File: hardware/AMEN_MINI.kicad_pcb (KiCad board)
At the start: 2 copper layers, 114.5 x 168.9 mm, 58 parts, among them J2 Conn_01x04_Pin, J3 Conn_01x14, J4 Conn_01x14, SW1 SW_Push_45deg, SW10 SW_Push_45deg, SW11 SW_Push_45deg, SW12 SW_Push_45deg, SW13 SW_Push_45deg, SW14 SW_Push_45deg, SW15 SW_Push_45deg, SW16 SW_Push_45deg, SW17 SW_Push_45deg, SW18 SW_Push_45deg, SW19 SW_Push_45deg, SW2 SW_Push_45deg, SW20 SW_Push_45deg, SW21 SW_Push_45deg, SW3 SW_Push_45deg, SW4 SW_Push_45deg, SW5 SW_Push_45deg, SW6 SW_Push_45deg, SW7 SW_Push_45deg, SW8 SW_Push_45deg, SW9 SW_Push_45deg, U2 Teensy4.1

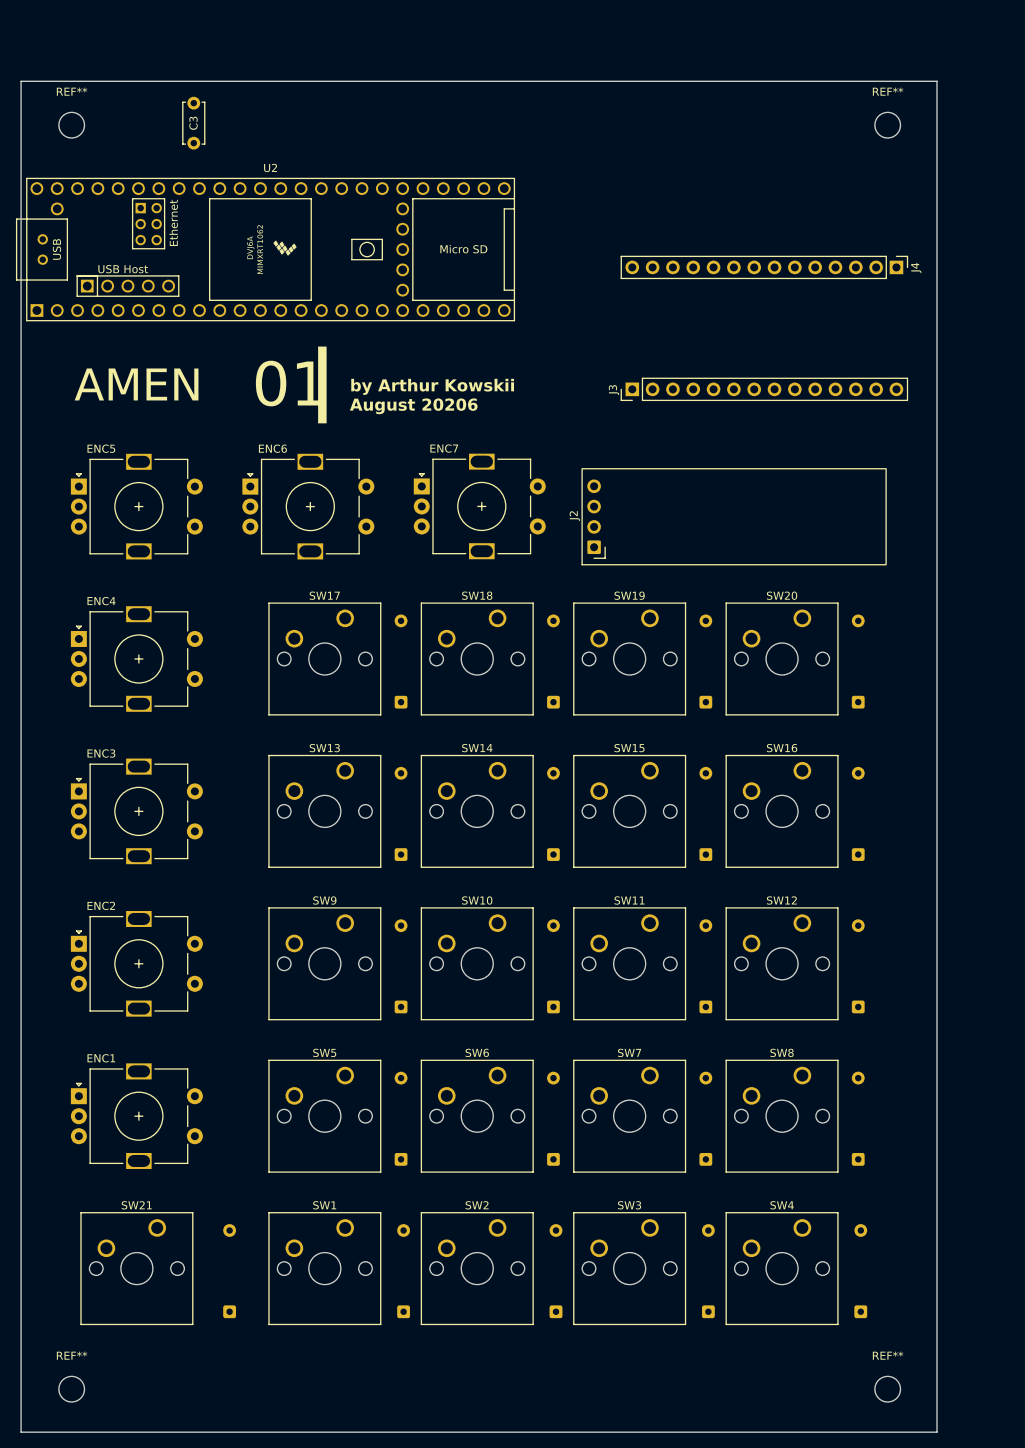
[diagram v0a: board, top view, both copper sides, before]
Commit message: Pre DRC connections
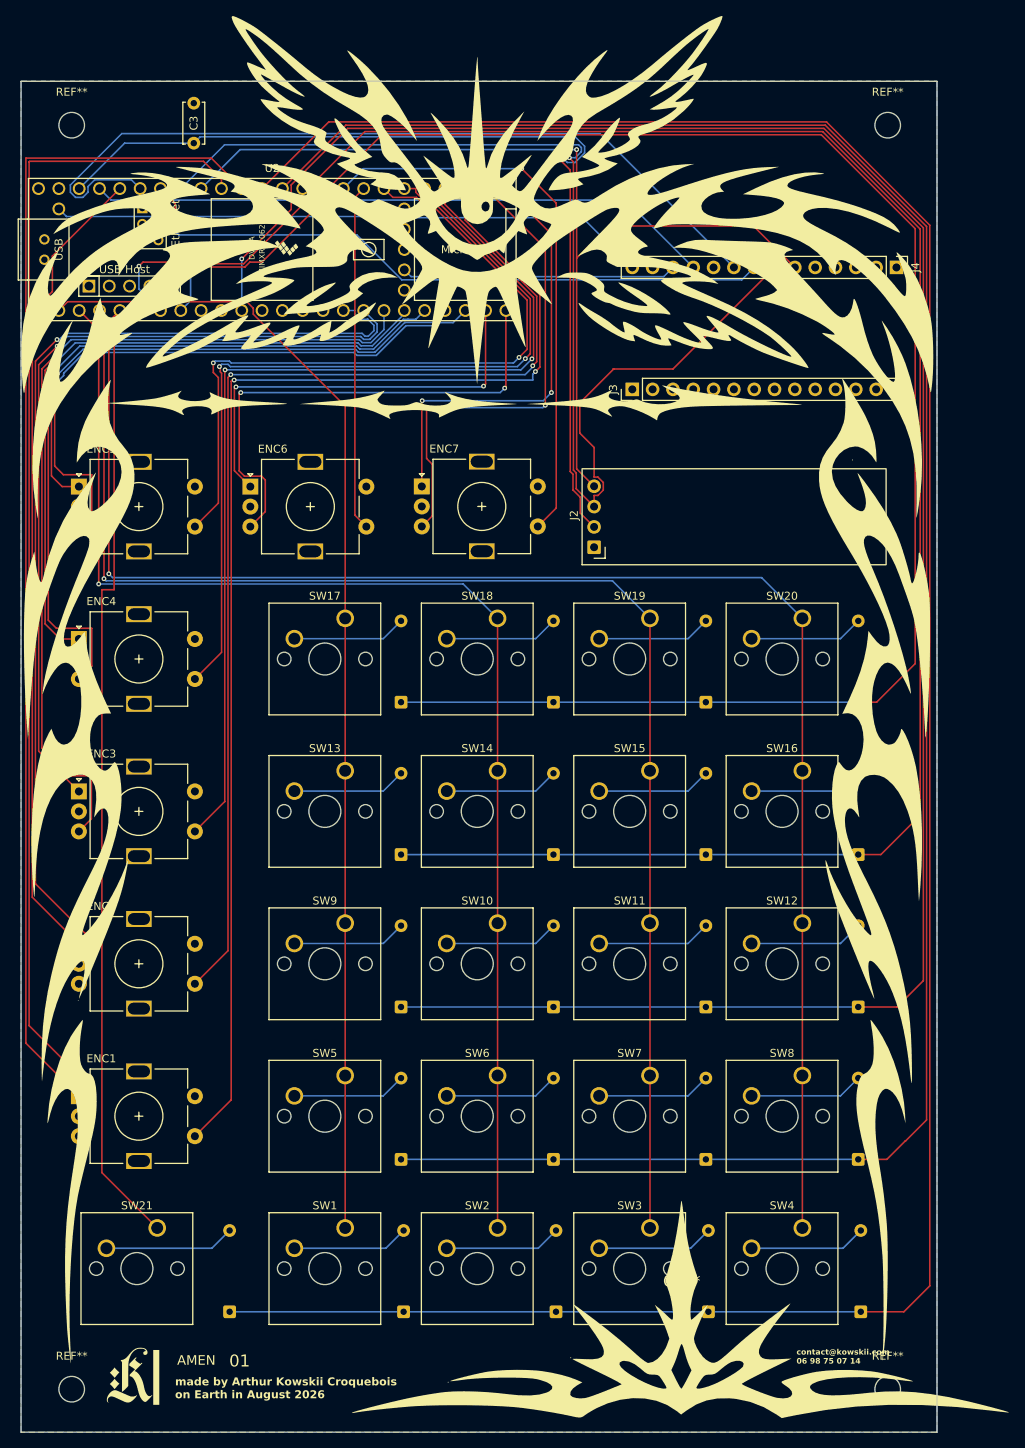
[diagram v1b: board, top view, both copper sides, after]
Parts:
- added G***: LOGO, LOGO, F.Cu at (56.2, 175.3)
- added G***: LOGO, LOGO, F.Cu at (99.7, 89.6)
- added G***: LOGO, LOGO, F.Cu at (96.6, 53.0)
- added G***: LOGO, LOGO, F.Cu at (125.3, 163.5)
- moved U2 0.20 mm to (74.1, 34.5)
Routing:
- net /ROW4: track 0.00 -> 313.7 mm
- net /ROW3: track 0.00 -> 268.5 mm
- net /ROW2: track 0.00 -> 266.1 mm, vias 0 -> 1
- net /ROW1: track 0.00 -> 250.3 mm, vias 0 -> 1
- net /ROW0: track 0.00 -> 237.4 mm, vias 0 -> 1
- net /COL3: track 0.00 -> 198.7 mm, vias 0 -> 1
- net /COL2: track 0.00 -> 180.3 mm, vias 0 -> 1
- net /COL1: track 0.00 -> 163.0 mm, vias 0 -> 1
- net /E1_SW: track 0.00 -> 162.2 mm, vias 0 -> 2
- net +3V3: track 0.00 -> 155.0 mm, vias 0 -> 2
- net /E1_B: track 0.00 -> 151.6 mm
- net /E1_A: track 0.00 -> 148.6 mm
- net /SCL: track 0.00 -> 146.4 mm, vias 0 -> 1
- net /COL0: track 0.00 -> 144.8 mm
- net /E2_SW: track 0.00 -> 143.4 mm, vias 0 -> 2
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- added copper zone on B.Cu, net GND
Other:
- board text added: "contact@kowskii.com 06 98 75 07 14"
- board text added: "made by Arthur Kowskii Croquebois on Earth in August 2026"
- board text removed: "by Arthur Kowskii August 20206"

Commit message: post DRC linking, 0 errors
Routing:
- net GND: track 0.00 -> 97.0 mm, vias 0 -> 4
- net /I2S_DOUT: track 0.00 -> 93.0 mm, vias 0 -> 1
- net /I2S_DIN: track 0.00 -> 90.1 mm, vias 0 -> 1
- net +3V3: track 155.0 -> 209.2 mm, vias 2 -> 3
- net /+5V_USB: track 74.7 -> 81.9 mm

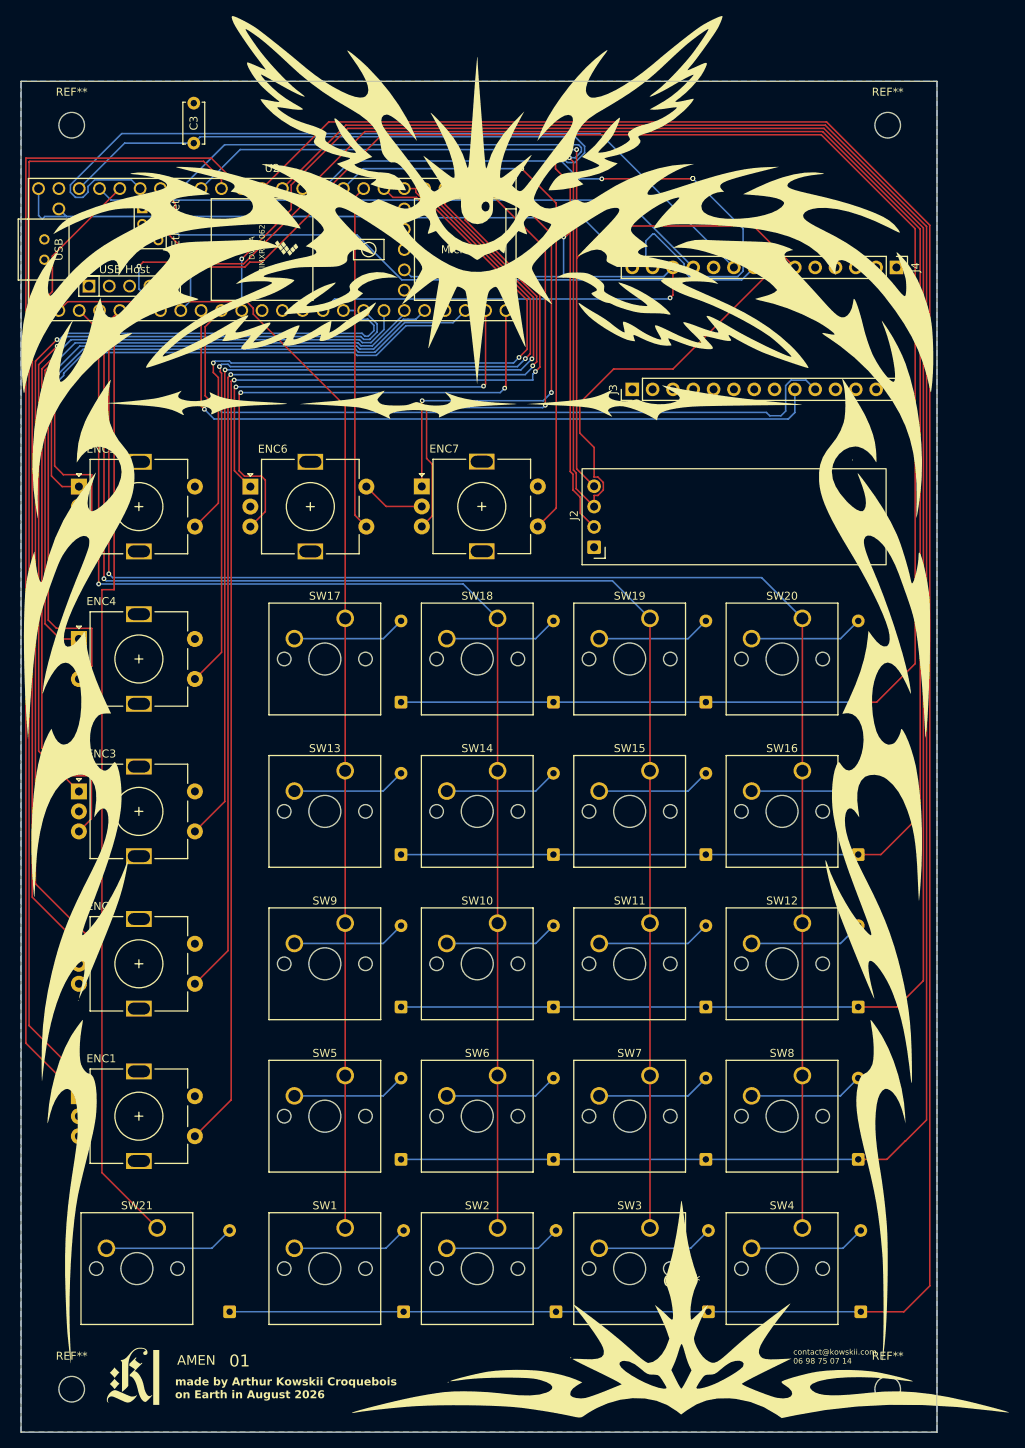
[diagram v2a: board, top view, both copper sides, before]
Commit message: fix(pcb): improve I2S routing and ground continuity
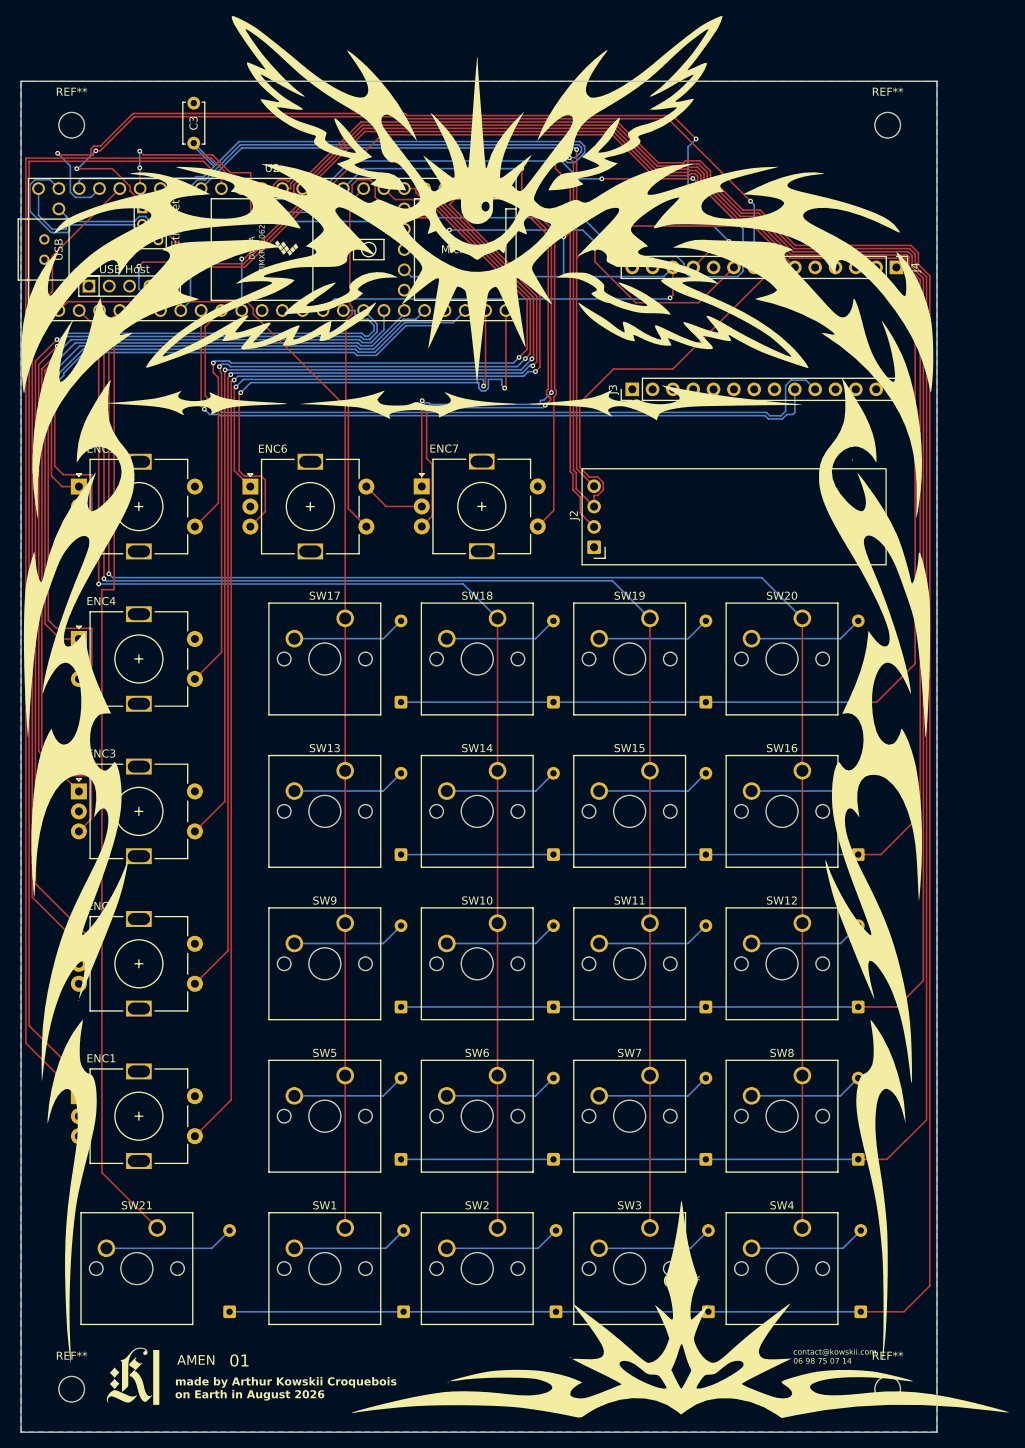
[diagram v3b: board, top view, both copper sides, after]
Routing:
- net /I2S_MCLK: track 78.3 -> 115.2 mm, vias 0 -> 3
- net /I2S_LRCLK: track 81.6 -> 112.5 mm, vias 1 -> 3
- net GND: track 97.0 -> 119.1 mm, vias 4 -> 3
- net +3V3: track 209.2 -> 216.9 mm
- net /I2S_BCLK: track 104.2 -> 97.7 mm, vias 0 -> 6
- net /+5V_USB: track 81.9 -> 85.5 mm
- net /E6_B: track 63.2 -> 66.4 mm
- net /E7_B: track 60.8 -> 63.1 mm
- net /ROW1: track 250.3 -> 248.1 mm
- net /ROW0: track 237.4 -> 235.4 mm
- net /ROW4: track 313.7 -> 312.0 mm
- net /ROW3: track 268.5 -> 266.8 mm
- net /ROW2: track 266.1 -> 264.7 mm
- net /E1_SW: track 162.2 -> 163.4 mm
- net /E6_SW: track 43.3 -> 44.5 mm
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
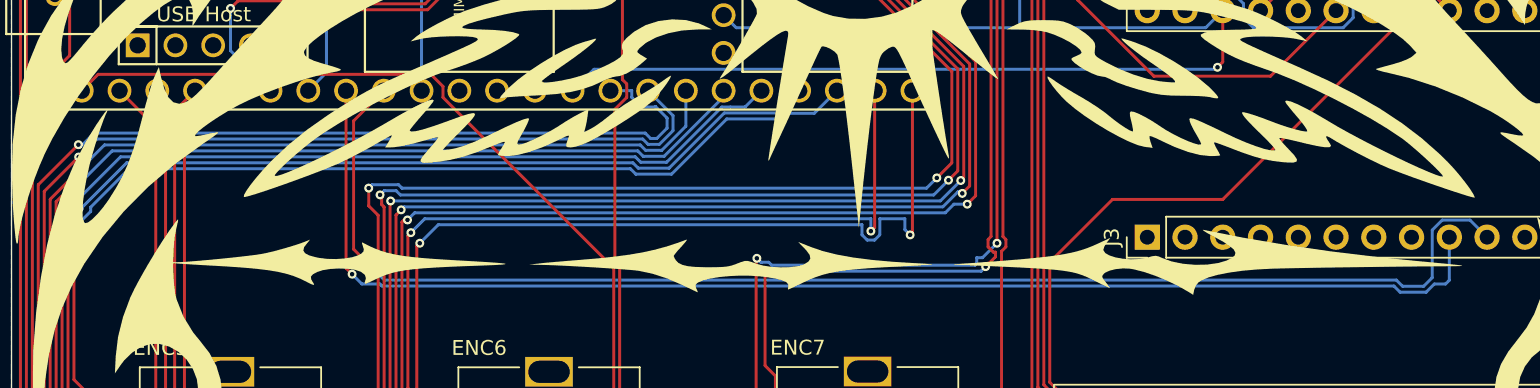
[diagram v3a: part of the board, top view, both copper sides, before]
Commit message: increasing gap between DIN & DOUT tracks
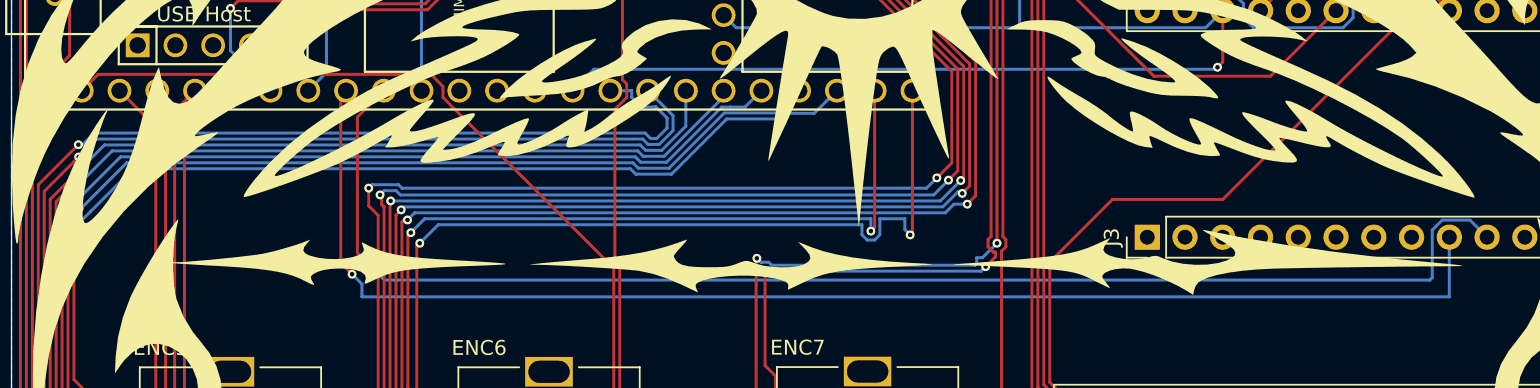
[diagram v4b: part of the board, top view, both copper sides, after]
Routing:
- net /I2S_DIN: track 90.1 -> 91.8 mm
- net /I2S_DOUT: track 93.0 -> 92.4 mm
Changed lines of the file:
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@@
-	)
-	(segment
-		(start 47.9964 50.286529)
-		(end 47.9964 50.003686)
-		(width 0.2)
-		(layer "B.Cu")
-		(net "/E5_B")
 	)
 	(segment
@@
 	)
 	(segment
+		(start 50.86773 47.4152)
+		(end 84.304259 47.4152)
+		(width 0.2)
+		(layer "B.Cu")
+		(net "/E5_B")
+	)
+	(segment
+		(start 47.9964 50.286529)
+		(end 50.86773 47.4152)
+		(width 0.2)
+		(layer "B.Cu")
+		(net "/E5_B")
+	)
+	(segment
+		(start 94.322086 44.064)
+		(end 94.698086 43.688)
+		(width 0.2)
+		(layer "B.Cu")
+		(net "/E5_B")
+	)
+	(segment
+		(start 90.786744 44.064)
+		(end 94.322086 44.064)
+		(width 0.2)
+		(layer "B.Cu")
+		(net "/E5_B")
+	)
+	(segment
+		(start 96.6724 43.688)
+		(end 98.1964 42.164)
+		(width 0.2)
+		(layer "B.Cu")
+		(net "/E5_B")
+	)
+	(segment
+		(start 84.667974 47.778914)
+		(end 87.07183 47.778914)
+		(width 0.2)
+		(layer "B.Cu")
+		(net "/E5_B")
+	)
+	(segment
 		(start 94.698086 43.688)
 		(end 96.6724 43.688)
@@
 	)
 	(segment
-		(start 96.6724 43.688)
-		(end 98.1964 42.164)
-		(width 0.2)
-		(layer "B.Cu")
-		(net "/E5_B")
-	)
-	(segment
-		(start 50.584886 47.4152)
-		(end 84.304259 47.4152)
-		(width 0.2)
-		(layer "B.Cu")
-		(net "/E5_B")
-	)
-	(segment
-		(start 90.786744 44.064)
-		(end 94.322086 44.064)
-		(width 0.2)
-		(layer "B.Cu")
-		(net "/E5_B")
-	)
-	(segment
-		(start 47.9964 50.003686)
-		(end 50.584886 47.4152)
+		(start 84.304259 47.4152)
+		(end 84.667974 47.778914)
 		(width 0.2)
 		(layer "B.Cu")
@@
 	)
 	(segment
-		(start 94.322086 44.064)
-		(end 94.698086 43.688)
-		(width 0.2)
-		(layer "B.Cu")
-		(net "/E5_B")
-	)
-	(segment
-		(start 84.667974 47.778914)
-		(end 87.07183 47.778914)
-		(width 0.2)
-		(layer "B.Cu")
-		(net "/E5_B")
-	)
-	(segment
-		(start 84.304259 47.4152)
-		(end 84.667974 47.778914)
-		(width 0.2)
-		(layer "B.Cu")
-		(net "/E5_B")
-	)
-	(segment
 		(start 105.9276 47.022338)
 		(end 105.9276 40.866572)
@@
 	)
 	(segment
-		(start 65.1764 54.102)
+		(start 64.8208 53.7464)
 		(end 65.5828 54.5084)
 		(width 0.2)
@@
 	(segment
 		(start 65.1764 42.164)
-		(end 65.1764 54.102)
+		(end 64.8208 42.5196)
 		(width 0.2)
 		(layer "F.Cu")
 		(net "/I2S_DIN")
 	)
+	(segment
+		(start 64.8208 42.5196)
+		(end 64.8208 53.7464)
+		(width 0.2)
+		(layer "F.Cu")
+		(net "/I2S_DIN")
+	)
 	(via
 		(at 65.5828 54.5084)
@@
 	)
 	(segment
-		(start 136.085861 55.7212)
-		(end 137.833686 55.7212)
+		(start 66.2432 56.0324)
+		(end 139.3952 56.0324)
 		(width 0.2)
 		(layer "B.Cu")
@@
 	)
 	(segment
-		(start 138.386086 55.1688)
-		(end 139.1412 55.1688)
+		(start 139.3952 56.0324)
+		(end 139.3952 52.0192)
+		(width 0.2)
+		(layer "B.Cu")
+		(net "/I2S_DIN")
+	)
+	(segment
+		(start 66.2432 55.1688)
+		(end 66.2432 56.0324)
 		(width 0.2)
 		(layer "B.Cu")
@@
 	)
 	(segment
-		(start 67.455515 55.1688)
-		(end 67.591915 55.3052)
-		(width 0.2)
-		(layer "B.Cu")
-		(net "/I2S_DIN")
-	)
-	(segment
-		(start 139.3952 54.9148)
-		(end 139.3952 52.0192)
-		(width 0.2)
-		(layer "B.Cu")
-		(net "/I2S_DIN")
-	)
-	(segment
-		(start 135.66986 55.3052)
-		(end 136.085861 55.7212)
-		(width 0.2)
-		(layer "B.Cu")
-		(net "/I2S_DIN")
-	)
-	(segment
-		(start 67.591915 55.3052)
-		(end 135.66986 55.3052)
-		(width 0.2)
-		(layer "B.Cu")
-		(net "/I2S_DIN")
-	)
-	(segment
-		(start 66.2432 55.1688)
-		(end 67.455515 55.1688)
-		(width 0.2)
-		(layer "B.Cu")
-		(net "/I2S_DIN")
-	)
-	(segment
-		(start 137.833686 55.7212)
-		(end 138.386086 55.1688)
-		(width 0.2)
-		(layer "B.Cu")
-		(net "/I2S_DIN")
-	)
-	(segment
-		(start 139.1412 55.1688)
-		(end 139.3952 54.9148)
-		(width 0.2)
-		(layer "B.Cu")
-		(net "/I2S_DIN")
-	)
-	(segment
-		(start 65.6844 52.832)
+		(start 67.7164 42.164)
+		(end 65.9384 43.942)
+		(width 0.2)
+		(layer "F.Cu")
+		(net "/I2S_DOUT")
+	)
+	(segment
+		(start 65.9384 43.942)
+		(end 65.9384 53.086)
+		(width 0.2)
+		(layer "F.Cu")
+		(net "/I2S_DOUT")
+	)
+	(segment
+		(start 65.9384 53.086)
 		(end 66.6496 53.7972)
-		(width 0.2)
-		(layer "F.Cu")
-		(net "/I2S_DOUT")
-	)
-	(segment
-		(start 65.6844 44.196)
-		(end 65.6844 52.832)
-		(width 0.2)
-		(layer "F.Cu")
-		(net "/I2S_DOUT")
-	)
-	(segment
-		(start 67.7164 42.164)
-		(end 65.6844 44.196)
 		(width 0.2)
 		(layer "F.Cu")
@@
 	)
 	(segment
+		(start 138.2452 51.542854)
+		(end 138.918854 50.8692)
+		(width 0.2)
+		(layer "B.Cu")
+		(net "/I2S_DOUT")
+	)
+	(segment
+		(start 140.7852 50.8692)
+		(end 141.9352 52.0192)
+		(width 0.2)
+		(layer "B.Cu")
+		(net "/I2S_DOUT")
+	)
+	(segment
+		(start 138.084 54.9052)
+		(end 138.2452 54.744)
+		(width 0.2)
+		(layer "B.Cu")
+		(net "/I2S_DOUT")
+	)
+	(segment
+		(start 66.6496 53.7972)
+		(end 67.7576 54.9052)
+		(width 0.2)
+		(layer "B.Cu")
+		(net "/I2S_DOUT")
+	)
+	(segment
+		(start 67.7576 54.9052)
+		(end 138.084 54.9052)
+		(width 0.2)
+		(layer "B.Cu")
+		(net "/I2S_DOUT")
+	)
+	(segment
 		(start 138.918854 50.8692)
 		(end 140.7852 50.8692)
 		(width 0.2)
 		(layer "B.Cu")
-		(net "/I2S_DOUT")
-	)
-	(segment
-		(start 137.668 55.3212)
-		(end 138.2452 54.744)
-		(width 0.2)
-		(layer "B.Cu")
-		(net "/I2S_DOUT")
-	)
-	(segment
-		(start 140.7852 50.8692)
-		(end 141.9352 52.0192)
-		(width 0.2)
-		(layer "B.Cu")
-		(net "/I2S_DOUT")
-	)
-	(segment
-		(start 138.2452 51.542854)
-		(end 138.918854 50.8692)
-		(width 0.2)
-		(layer "B.Cu")
-		(net "/I2S_DOUT")
-	)
-	(segment
-		(start 136.251546 55.3212)
-		(end 137.668 55.3212)
-		(width 0.2)
-		(layer "B.Cu")
-		(net "/I2S_DOUT")
-	)
-	(segment
-		(start 67.7576 54.9052)
-		(end 135.835546 54.9052)
-		(width 0.2)
-		(layer "B.Cu")
-		(net "/I2S_DOUT")
-	)
-	(segment
-		(start 66.6496 53.7972)
-		(end 67.7576 54.9052)
-		(width 0.2)
-		(layer "B.Cu")
-		(net "/I2S_DOUT")
-	)
-	(segment
-		(start 135.835546 54.9052)
-		(end 136.251546 55.3212)
-		(width 0.2)
-		(layer "B.Cu")
